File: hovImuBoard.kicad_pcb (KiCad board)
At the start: 2 copper layers, 71.6 x 71.6 mm, 67 parts, among them J1 AVR-ISP-6, J2 Ext. Power, J3 54602-908LF, J4 AVR-JTAG-10, J5 ExtensionPort, J6 Debug, U1 LD2981, U2 BMX160, U3 SN65HVD32DR, U4 ATmega1284P-AU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

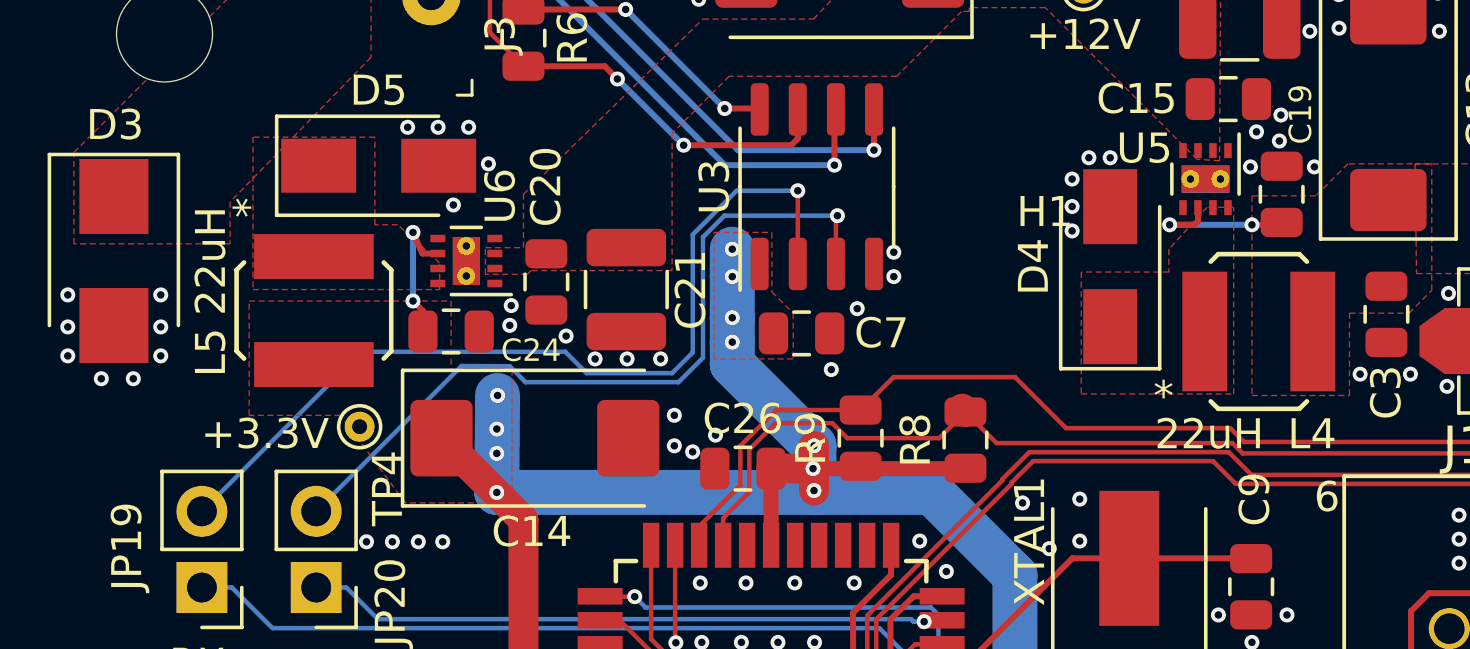
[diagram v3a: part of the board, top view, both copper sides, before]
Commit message: Correct L4 and L5 to 2.2uH. Update BOM
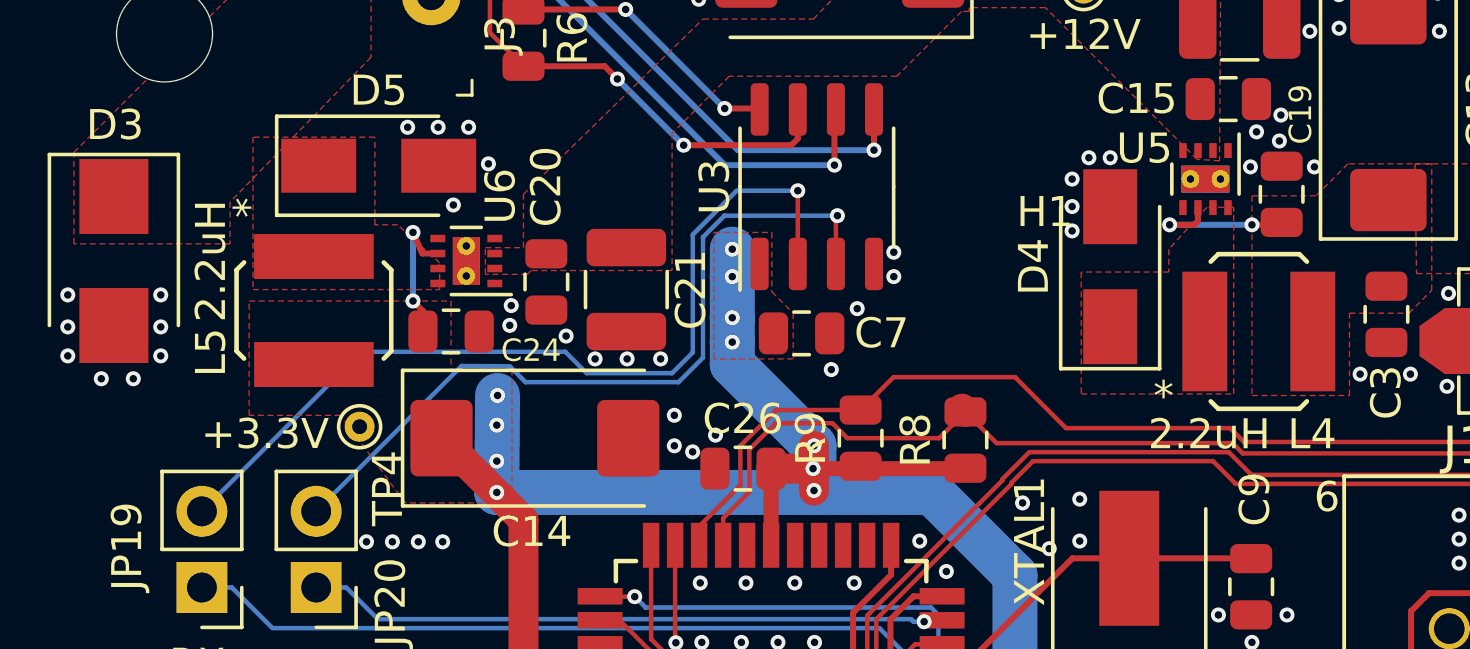
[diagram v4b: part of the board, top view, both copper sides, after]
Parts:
- L4, L5: value 22uH -> 2.2uH
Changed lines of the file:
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@@
     (add_net "Net-(D4-Pad1)")
     (add_net "Net-(D5-Pad1)")
+    (add_net "Net-(J4-Pad7)")
+    (add_net "Net-(J4-Pad8)")
     (add_net "Net-(JP17-Pad2)")
     (add_net "Net-(JP19-Pad1)")
     (add_net "Net-(JP20-Pad1)")
     (add_net "Net-(L1-Pad1)")
+    (add_net "Net-(U2-Pad10)")
+    (add_net "Net-(U2-Pad11)")
+    (add_net "Net-(U2-Pad4)")
+    (add_net "Net-(U2-Pad9)")
+    (add_net "Net-(U4-Pad13)")
+    (add_net "Net-(U4-Pad14)")
+    (add_net "Net-(U4-Pad15)")
+    (add_net "Net-(U4-Pad16)")
+    (add_net "Net-(U4-Pad25)")
+    (add_net "Net-(U4-Pad26)")
+    (add_net "Net-(U4-Pad29)")
+    (add_net "Net-(U4-Pad30)")
+    (add_net "Net-(U4-Pad31)")
+    (add_net "Net-(U4-Pad32)")
+    (add_net "Net-(U4-Pad33)")
+    (add_net "Net-(U4-Pad34)")
+    (add_net "Net-(U4-Pad35)")
+    (add_net "Net-(U4-Pad36)")
+    (add_net "Net-(U4-Pad37)")
+    (add_net "Net-(U4-Pad44)")
+    (add_net "Net-(U5-Pad8)")
+    (add_net "Net-(U6-Pad8)")
   )
   (net_class PWR2Pad ""
@@
       (effects (font (size 1 1) (thickness 0.15)))
     )
-    (fp_text value 22uH (at -1.651 3.429 90) (layer F.SilkS)
+    (fp_text value 2.2uH (at -1.651 3.429 90) (layer F.SilkS)
       (effects (font (size 1 1) (thickness 0.15)))
     )
@@
       (effects (font (size 1 1) (thickness 0.15)))
     )
-    (fp_text value 22uH (at -1.651 3.429 180) (layer F.SilkS)
+    (fp_text value 2.2uH (at -1.651 3.429 180) (layer F.SilkS)
       (effects (font (size 1 1) (thickness 0.15)))
     )
@@
   (gr_line (start 74 127.4) (end 128 127.4) (layer Edge.Cuts) (width 0.05))
   (gr_line (start 65.2 64.6) (end 65.2 118.6) (layer Edge.Cuts) (width 0.05))
-  (via (at 114.8 103) (size 0.5) (drill 0.25) (layers F.Cu B.Cu) (net 2) (status 40000))
-  (via (at 114.8 102.2) (size 0.5) (drill 0.25) (layers F.Cu B.Cu) (net 2) (status 40000))
-  (via (at 127.2 102.2) (size 0.5) (drill 0.25) (layers F.Cu B.Cu) (net 2) (status 40000))
-  (via (at 127.2 103) (size 0.5) (drill 0.25) (layers F.Cu B.Cu) (net 2) (status 40000))
-  (via (at 127.2 103.8) (size 0.5) (drill 0.25) (layers F.Cu B.Cu) (net 2) (status 40000))
   (via (at 79.931 95.062) (size 0.5) (drill 0.25) (layers F.Cu B.Cu) (net 1))
   (via (at 79.931 92.776) (size 0.5) (drill 0.25) (layers F.Cu B.Cu) (net 1))
@@
   (segment (start 90.5736 96.4336) (end 90.5736 95.6208) (width 1.5) (layer B.Cu) (net 1))
   (via (at 90.5736 96.4336) (size 0.5) (drill 0.25) (layers F.Cu B.Cu) (net 1))
-  (via (at 82.725 100.142) (size 0.5) (drill 0.25) (layers F.Cu B.Cu) (net 1))
-  (via (at 82.725 99.3292) (size 0.5) (drill 0.25) (layers F.Cu B.Cu) (net 1))
+  (via (at 82.725 100.4) (size 0.5) (drill 0.25) (layers F.Cu B.Cu) (net 1))
+  (via (at 82.725 99.2) (size 0.5) (drill 0.25) (layers F.Cu B.Cu) (net 1))
   (segment (start 82.7504 98.2116) (end 82.725 101.44425) (width 1.5) (layer B.Cu) (net 1))
   (via (at 82.7504 98.2116) (size 0.5) (drill 0.25) (layers F.Cu B.Cu) (net 1))
@@
   (segment (start 114.4432 117.0432) (end 119.5568 117.0432) (width 1) (layer B.Cu) (net 1))
   (segment (start 119.5568 117.0432) (end 121 115.6) (width 1) (layer B.Cu) (net 1))
+  (via (at 114.8 103) (size 0.5) (drill 0.25) (layers F.Cu B.Cu) (net 2) (status 40000))
+  (via (at 114.8 102.2) (size 0.5) (drill 0.25) (layers F.Cu B.Cu) (net 2) (status 40000))
+  (via (at 127.2 102.2) (size 0.5) (drill 0.25) (layers F.Cu B.Cu) (net 2) (status 40000))
+  (via (at 127.2 103) (size 0.5) (drill 0.25) (layers F.Cu B.Cu) (net 2) (status 40000))
+  (via (at 127.2 103.8) (size 0.5) (drill 0.25) (layers F.Cu B.Cu) (net 2) (status 40000))
   (via (at 121.46 94.6048) (size 0.5) (drill 0.25) (layers F.Cu B.Cu) (net 2))
   (via (at 121.0028 95.3668) (size 0.5) (drill 0.25) (layers F.Cu B.Cu) (net 2))
@@
   (via (at 130.6792 110.9472) (size 0.5) (drill 0.25) (layers F.Cu B.Cu) (net 2))
   (via (at 109 110.271613) (size 0.5) (drill 0.25) (layers F.Cu B.Cu) (net 2))
+  (via (at 114.8 103.8) (size 0.5) (drill 0.25) (layers F.Cu B.Cu) (net 2) (status 40000))
   (via (at 118.666 91.3536) (size 0.5) (drill 0.25) (layers F.Cu B.Cu) (net 4))
   (via (at 105.1532 92.522) (size 0.5) (drill 0.25) (layers F.Cu B.Cu) (net 4))
@@
   (segment (start 113.2 105.4) (end 113.2 105.8) (width 0.2) (layer F.Cu) (net 18))
   (segment (start 113.2 105.8) (end 113.2 114) (width 0.2) (layer F.Cu) (net 18))
-  (via (at 114.8 103.8) (size 0.5) (drill 0.25) (layers F.Cu B.Cu) (net 2) (status 40000))
   (segment (start 113.2 105.8) (end 113.2 105.8) (width 0.2) (layer F.Cu) (net 18))
   (segment (start 130.051 108.651) (end 131.7305 108.651) (width 0.2) (layer F.Cu) (net 18))

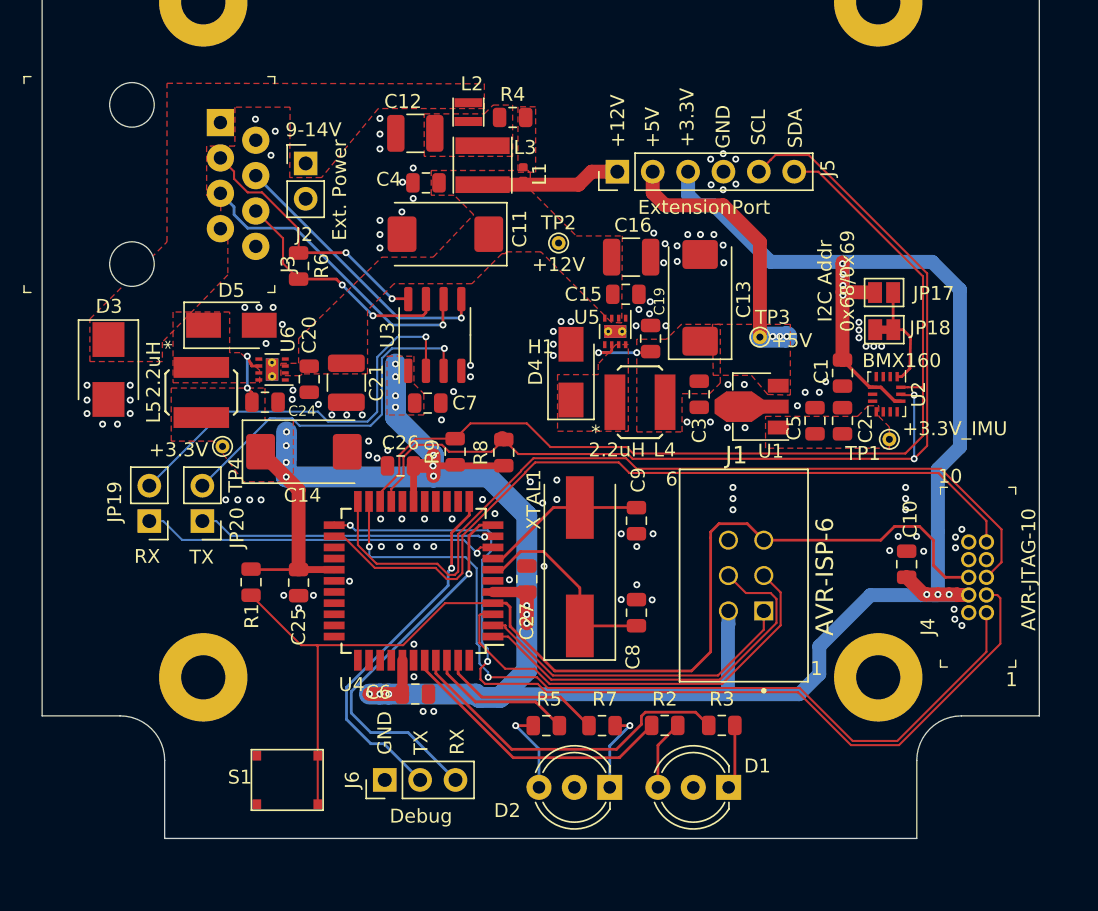
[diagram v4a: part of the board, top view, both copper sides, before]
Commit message: Optimize the layout.
Re-route tracks inside the screw hole.
Remove some vias connecting the ground planes.
Re-route tracks inside the ATMega to allow better connection between ground planes.
Overlay ground copper zones to add thermal relief to manually soldered items.
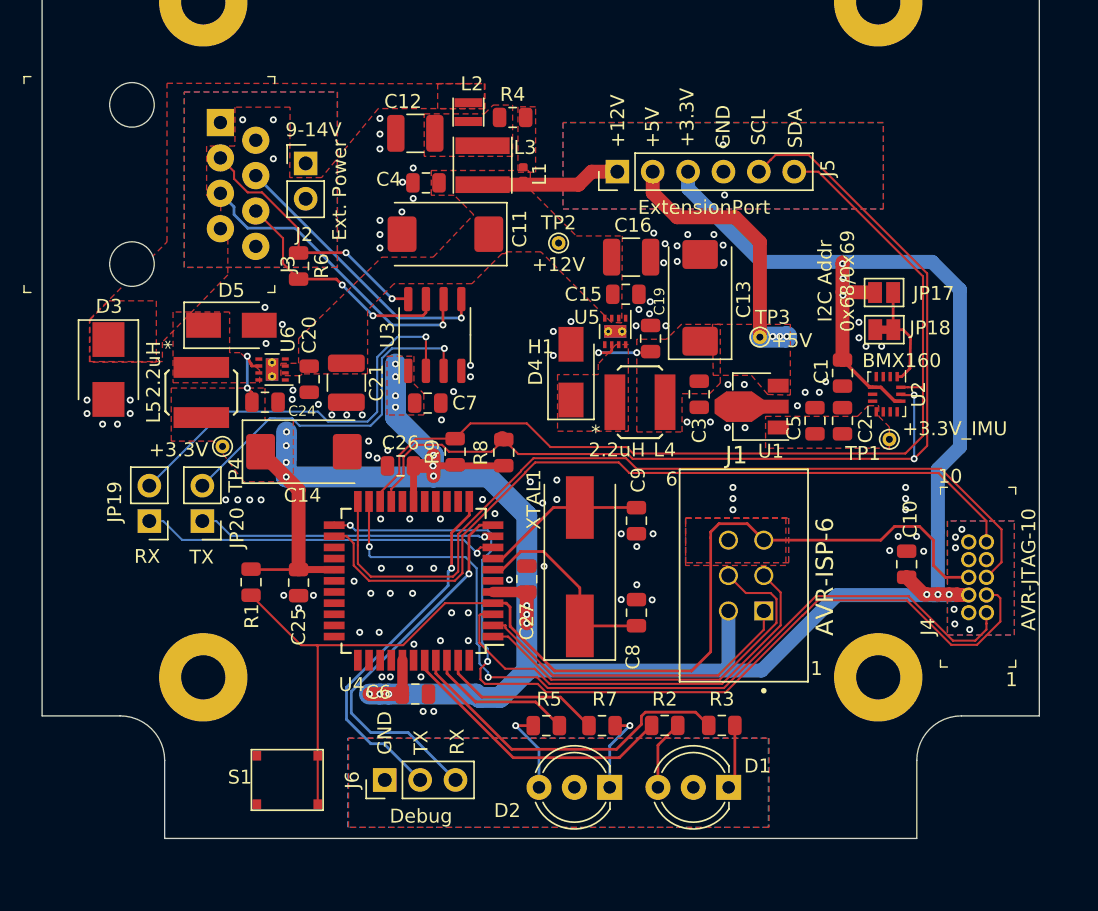
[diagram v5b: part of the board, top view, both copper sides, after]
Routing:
- net +3V3: track 207.4 -> 201.8 mm, vias 26 -> 25
- net /JTAG_TDI: track 56.4 -> 58.1 mm
- net /JTAG_TDO: track 69.5 -> 68.1 mm
- net /JTAG_TCK: track 63.3 -> 61.8 mm
- net /JTAG_TMS: track 61.3 -> 62.2 mm
- net GND: vias 132 -> 128
